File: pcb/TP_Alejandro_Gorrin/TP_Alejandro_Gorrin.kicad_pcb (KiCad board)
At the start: 2 copper layers, 33 parts, among them J1 Conn_01x12, J2 Conn_01x02, J3 Conn_01x16, J4 USB_A, Q1 MMBT3904, Q2 MMBT3904, Q3 BS250, SW1 SW_1, U1 MCP73831-2-OT, U3 CP2104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

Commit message: Empezando con el ruteo
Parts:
- moved U4 61.7 mm to (129.0, 88.0)
- moved J3 56.7 mm to (147.0, 123.0), turned to 90 degrees
- moved C6 53.7 mm to (128.0, 82.0), turned to 270 degrees
- moved R13 51.0 mm to (155.0, 82.0)
- moved C1 47.6 mm to (128.0, 105.0), turned to 90 degrees
- moved Q2 44.7 mm to (145.0, 115.0), turned to 90 degrees
- moved C2 44.7 mm to (123.5, 113.0), turned to 180 degrees
- moved D4 39.2 mm to (133.0, 82.0), turned to 270 degrees
- moved HS1 37.7 mm to (175.0, 110.0), turned to 270 degrees
- moved R4 36.4 mm to (151.7, 92.0)
- moved U5 36.3 mm to (155.0, 100.0)
- moved R3 34.8 mm to (147.0, 92.0)
- moved J2 31.3 mm to (144.0, 83.0), turned to 90 degrees
- moved R7 30.2 mm to (124.0, 88.3), turned to 270 degrees
- moved R10 29.2 mm to (159.3, 110.0), turned to 180 degrees
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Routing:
- net GNDD: track 0.00 -> 54.6 mm
- net +3V3: track 0.00 -> 26.9 mm
- net /RESET: track 0.00 -> 10.2 mm
- net +BATT: track 0.00 -> 9.84 mm
- net Net-(Q2-Pad1): track 0.00 -> 7.39 mm
- net Net-(R1-Pad2): track 0.00 -> 7.19 mm
- net VBUS: track 0.00 -> 5.75 mm
- net Net-(Q1-Pad1): track 0.00 -> 5.23 mm
- net /RTS: track 0.00 -> 4.62 mm
- net Net-(C6-Pad1): track 0.00 -> 4.29 mm
- net Net-(D1-Pad1): track 0.00 -> 4.17 mm
- net /A13_I35: track 0.00 -> 4.04 mm
- net Net-(R7-Pad2): track 0.00 -> 4.03 mm
- net /DTR: track 0.00 -> 3.73 mm
- net Net-(D3-Pad2): track 0.00 -> 3.03 mm
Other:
- board outline added: 79 x 47 mm
- net class Prueba added: clearance 0.8, trace_width 0.8, via_dia 1.6, via_drill 0.8

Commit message: vias del PCB
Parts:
- moved U5 1.41 mm to (156.0, 101.0), turned to 270 degrees
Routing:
- net VBUS: track 5.75 -> 106.8 mm, vias 0 -> 9
- net GNDD: track 54.6 -> 124.4 mm, vias 0 -> 9
- net +BATT: track 9.84 -> 77.7 mm, vias 0 -> 3
- net +3V3: track 26.9 -> 74.2 mm, vias 0 -> 3
- net /RESET: track 10.2 -> 43.6 mm, vias 0 -> 1
- net /RTS: track 4.62 -> 33.1 mm, vias 0 -> 2
- net /DTR: track 3.73 -> 29.4 mm
- net Net-(J4-Pad2): track 0.00 -> 22.8 mm, vias 0 -> 1
- net Net-(J4-Pad3): track 0.00 -> 21.6 mm, vias 0 -> 1
- net Net-(C6-Pad1): track 4.29 -> 23.0 mm, vias 0 -> 1
- net Net-(J4-Pad5): track 0.00 -> 13.1 mm
- net Net-(R2-Pad1): track 0.00 -> 6.94 mm, vias 0 -> 2

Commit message: Cambios del Esquematico
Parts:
- C1: footprint Connector_USB:USB_A_CONNFLY_DS1095-WNR0 -> Capacitor_SMD:C_0805_2012Metric
- C2, C3, C4, C6, C7, C8: footprint Capacitor_SMD:CP_Elec_3x5.3 -> Capacitor_SMD:C_0805_2012Metric
- D1, D3, D4: footprint LED_SMD:LED_0603_1608Metric -> LED_SMD:LED_0805_2012Metric
- R1, R10, R12, R13, R13G1, R13G2, R2, R3, R4, R7: footprint Resistor_SMD:R_0201_0603Metric -> Resistor_SMD:R_0805_2012Metric
- SW1: footprint Button_Switch_SMD:SW_DIP_SPSTx01_Slide_6.7x4.1mm_W6.73mm_P2.54mm_LowProfile_JPin -> Button_Switch_SMD:SW_Push_1P1T_NO_6x6mm_H9.5mm
- U5: value ESP3212 -> ESP32-WROOM; footprint ESP32-footprints-Lib:ESP32 -> ESP32-footprints-Lib:ESP32-WROOM
- moved D1 79.5 mm to (198.1, 65.1), turned to 0 degrees
- moved R13G2 73.0 mm to (202.5, 65.1), turned to 0 degrees
- moved R13G1 70.5 mm to (198.1, 68.1)
- moved D4 61.2 mm to (193.5, 72.3), turned to 0 degrees
- moved J3 60.8 mm to (126.0, 65.9), turned to 0 degrees
- moved J2 52.4 mm to (193.6, 65.9), turned to 0 degrees
- moved R12 49.6 mm to (176.6, 92.9)
- moved R10 48.7 mm to (193.4, 75.3), turned to 0 degrees
- moved R7 43.8 mm to (164.7, 104.3), turned to 0 degrees
- moved U4 43.4 mm to (172.0, 93.7)
- moved R1 39.5 mm to (164.7, 98.4)
- moved HS1 38.2 mm to (155.2, 77.3), turned to 0 degrees
- moved R2 38.1 mm to (171.8, 97.5)
- moved U5 33.4 mm to (180.3, 78.1), turned to 0 degrees
- moved C1 32.3 mm to (160.3, 104.5), turned to 0 degrees
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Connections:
- R1 pad 1: GNDD -> Net-(R1-Pad1)
- R1 pad 2: Net-(R1-Pad2) -> GNDD
- U1 pad 5: Net-(R1-Pad2) -> Net-(R1-Pad1)
- U5 pad 10: /A0_DAC2 -> /A1_DAC1
- U5 pad 11: /IO27_A10 -> /A0_DAC2
- U5 pad 12: /IO14_A6 -> /IO27_A10
- U5 pad 13: /IO12_A11 -> /IO14_A6
- U5 pad 14: /IO13_A12 -> /IO12_A11
- U5 pad 15: /IO15_A8 -> GNDD
- U5 pad 16: Net-(U5-Pad16) -> /IO13_A12
- U5 pad 17: /GPIO2 -> Net-(U5-Pad17)
- U5 pad 18: /GPIO0 -> Net-(U5-Pad18)
- U5 pad 19: /A5_IO4 -> Net-(U5-Pad19)
- U5 pad 2: /RESET -> +3V3
- U5 pad 20: /IO16 -> Net-(U5-Pad20)
- U5 pad 21: +3V3 -> Net-(U5-Pad21)
- U5 pad 22: /IO17 -> Net-(U5-Pad22)
- U5 pad 23: /SCK -> /IO15_A8
- U5 pad 24: /MISI -> /GPIO2
- U5 pad 25: /SDA -> /GPIO0
- U5 pad 26: /MISO -> /A5_IO4
- U5 pad 27: /SCI -> /IO16
- U5 pad 28: /RXD0 -> /IO17
- U5 pad 29: /TXD0 -> /SCK
- U5 pad 3: /A4_IO36 -> /RESET
- U5 pad 30: /IO21 -> /MISI
- U5 pad 31: Net-(U5-Pad31) -> /MISO
- U5 pad 32: (no net) -> Net-(U5-Pad32)
- U5 pad 33: (no net) -> /IO21
- U5 pad 34: (no net) -> /RXD0
- U5 pad 35: (no net) -> /TXD0
- U5 pad 36: (no net) -> /SCI
- U5 pad 37: (no net) -> /SDA
- U5 pad 38: (no net) -> Net-(U5-Pad38)
- U5 pad 39: (no net) -> Net-(U5-Pad39)
- U5 pad 4: /A3_I39 -> /A4_IO36
- U5 pad 5: /A2_I34 -> /A3_I39
- U5 pad 6: /A13_I35 -> /A2_I34
- U5 pad 7: /IO32_A7 -> /A13_I35
- U5 pad 8: /IO33_A9 -> /IO32_A7
- U5 pad 9: /A1_DAC1 -> /IO33_A9
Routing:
- net GNDD: track 124.4 -> 0.00 mm, vias 9 -> 0
- net VBUS: track 106.8 -> 0.00 mm, vias 9 -> 0
- net +BATT: track 77.7 -> 0.00 mm, vias 3 -> 0
- net +3V3: track 74.2 -> 0.00 mm, vias 3 -> 0
- net /RESET: track 43.6 -> 0.00 mm, vias 1 -> 0
- net /RTS: track 33.1 -> 0.00 mm, vias 2 -> 0
- net /DTR: track 29.4 -> 0.00 mm
- net Net-(C6-Pad1): track 23.0 -> 0.00 mm, vias 1 -> 0
- net Net-(J4-Pad2): track 22.8 -> 0.00 mm, vias 1 -> 0
- net Net-(J4-Pad3): track 21.6 -> 0.00 mm, vias 1 -> 0
- net Net-(J4-Pad5): track 13.1 -> 0.00 mm
- net Net-(Q2-Pad1): track 7.39 -> 0.00 mm
- net Net-(R1-Pad2): track 7.19 -> 0.00 mm
- net Net-(R2-Pad1): track 6.94 -> 0.00 mm, vias 2 -> 0
- net Net-(Q1-Pad1): track 5.23 -> 0.00 mm
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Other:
- board outline removed
- net class Default: clearance 0.2 -> 0.1
- rule trace_clearance: 0.2 -> 0.1

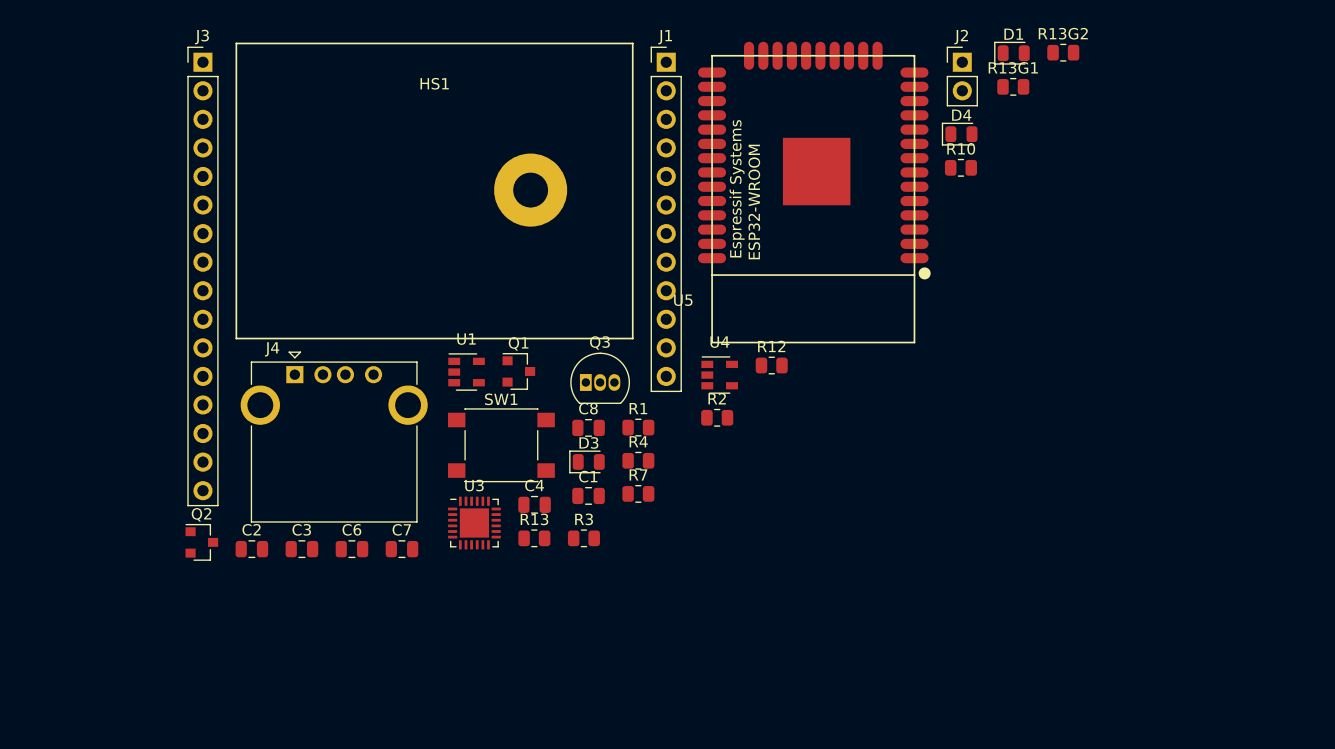
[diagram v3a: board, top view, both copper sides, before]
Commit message: Agrego avances de PCB, problemas con el heatsink
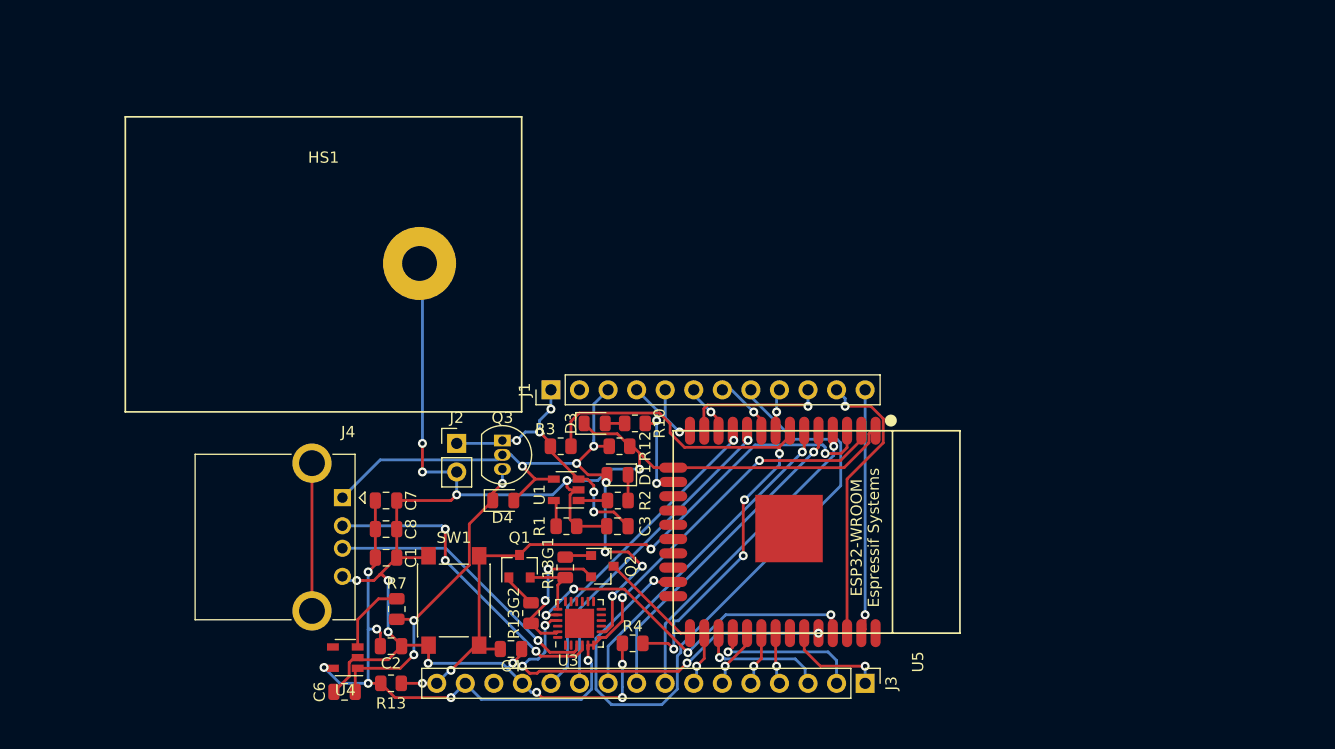
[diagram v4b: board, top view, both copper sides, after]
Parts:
- moved J3 80.7 mm to (184.9, 121.2), turned to 270 degrees
- moved R13G2 68.7 mm to (155.2, 114.9), turned to 270 degrees
- moved R13G1 58.4 mm to (158.2, 110.8), turned to 270 degrees
- moved J2 56.3 mm to (148.6, 99.8)
- moved D4 52.2 mm to (152.7, 104.9)
- moved D1 51.5 mm to (162.9, 102.6), turned to 180 degrees
- moved U4 41.7 mm to (138.7, 118.9), turned to 180 degrees
- moved R10 36.8 mm to (164.4, 98.0)
- moved Q2 35.7 mm to (161.5, 110.7)
- moved J1 30.9 mm to (157.0, 95.1), turned to 90 degrees
- moved U5 29.6 mm to (180.6, 107.7), turned to 90 degrees
- moved C3 28.1 mm to (162.9, 107.2)
- moved R7 23.8 mm to (143.3, 114.6), turned to 90 degrees
- moved C8 20.1 mm to (142.3, 107.4)
- moved C1 18.8 mm to (142.3, 110.0)
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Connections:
- R10 pad 2: /IO13_A1 -> /IO13_A12
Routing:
- net GNDD: track 0.00 -> 145.7 mm, vias 0 -> 13
- net +3V3: track 0.00 -> 84.5 mm, vias 0 -> 8
- net /IO15_A8: track 0.00 -> 60.2 mm, vias 0 -> 2
- net VBUS: track 0.00 -> 59.7 mm, vias 0 -> 7
- net /RESET: track 0.00 -> 57.8 mm, vias 0 -> 4
- net /A13_I35: track 0.00 -> 49.7 mm, vias 0 -> 4
- net /RXD0: track 0.00 -> 34.3 mm, vias 0 -> 4
- net /TXD0: track 0.00 -> 32.8 mm, vias 0 -> 4
- net /A2_I34: track 0.00 -> 29.7 mm, vias 0 -> 1
- net /A0_DAC2: track 0.00 -> 29.2 mm, vias 0 -> 1
- net /A3_I39: track 0.00 -> 29.2 mm, vias 0 -> 1
- net Net-(C6-Pad1): track 0.00 -> 29.0 mm, vias 0 -> 3
- net /A4_IO36: track 0.00 -> 28.7 mm, vias 0 -> 1
- net /A1_DAC1: track 0.00 -> 28.7 mm, vias 0 -> 1
- net Net-(J4-Pad2): track 0.00 -> 28.4 mm, vias 0 -> 3
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
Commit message: PCB
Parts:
- moved C2 53.6 mm to (195.3, 107.3), turned to 90 degrees
- moved U4 53.5 mm to (185.9, 93.7), turned to 90 degrees
- moved R13 50.6 mm to (189.8, 102.6)
- moved C7 50.5 mm to (192.5, 99.6), turned to 270 degrees
- moved C6 48.5 mm to (180.8, 98.0), turned to 90 degrees
- moved C8 48.3 mm to (190.0, 99.6), turned to 270 degrees
- moved R7 47.5 mm to (187.7, 97.9)
- moved J2 46.2 mm to (194.6, 95.5), turned to 270 degrees
- moved C1 45.1 mm to (186.9, 103.7), turned to 270 degrees
- moved C4 38.7 mm to (189.8, 104.9), turned to 180 degrees
- moved SW1 38.7 mm to (186.9, 111.3)
- moved R3 37.5 mm to (195.3, 99.4), turned to 270 degrees
- moved J4 37.5 mm to (175.8, 101.5)
- moved U3 34.9 mm to (194.3, 113.3), turned to 270 degrees
- moved R4 34.3 mm to (195.3, 103.2), turned to 270 degrees
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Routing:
- net /IO15_A8: track 60.2 -> 22.9 mm, vias 2 -> 1
- net /TXD0: track 32.8 -> 0.00 mm, vias 4 -> 0
- net /A13_I35: track 49.7 -> 19.4 mm, vias 4 -> 2
- net /A2_I34: track 29.7 -> 0.00 mm, vias 1 -> 0
- net /A0_DAC2: track 29.2 -> 0.00 mm, vias 1 -> 0
- net /A3_I39: track 29.2 -> 0.00 mm, vias 1 -> 0
- net /A4_IO36: track 28.7 -> 0.00 mm, vias 1 -> 0
- net /A1_DAC1: track 28.7 -> 0.00 mm, vias 1 -> 0
- net /SCI: track 26.0 -> 0.00 mm, vias 1 -> 0
- net /SDA: track 21.8 -> 0.00 mm, vias 1 -> 0
- net +3V3: track 84.5 -> 68.8 mm, vias 8 -> 3
- net /RXD0: track 34.3 -> 19.2 mm, vias 4 -> 2
- net /GPIO0: track 9.26 -> 24.0 mm, vias 0 -> 2
- net GNDD: track 145.7 -> 131.1 mm, vias 13 -> 10
- net /IO17: track 13.8 -> 0.00 mm, vias 1 -> 0
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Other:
- net class Default: clearance 0.1 -> 0.2
- rule trace_clearance: 0.1 -> 0.2

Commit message: Avances PCB
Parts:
- removed HS1: Heatsink_Pad, Heatsink:Heatsink_35x26mm_1xFixation3mm_Fischer-SK486-35
- J4: value USB_A -> USB_B_Micro; footprint Connector_USB:USB_A_CONNFLY_DS1095-WNR0 -> Connector_USB:USB_Micro-B_Molex_47346-0001
- moved J2 60.2 mm to (135.4, 84.3)
- moved C3 54.5 mm to (129.5, 85.0)
- moved C1 50.0 mm to (137.4, 96.6)
- moved C2 50.0 mm to (145.8, 100.1)
- moved C4 50.0 mm to (140.3, 97.8)
- moved C7 50.0 mm to (143.0, 92.5)
- moved C8 50.0 mm to (140.5, 92.5)
- moved D3 50.0 mm to (143.3, 100.2)
- moved J1 50.0 mm to (140.2, 84.3)
- moved J3 50.0 mm to (130.0, 111.8)
- moved Q1 50.0 mm to (132.1, 103.9)
- moved Q2 50.0 mm to (129.8, 107.7)
- moved R10 50.0 mm to (143.3, 96.4)
- moved R13 50.0 mm to (140.3, 95.5)
- moved R13G1 50.0 mm to (132.8, 107.8)
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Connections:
- J4 pad 4: GNDD -> Net-(J4-Pad4)
- J4 pad 5: Net-(J4-Pad5) -> GNDD
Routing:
- net Net-(J4-Pad5): track 13.1 -> 0.00 mm
- net Net-(J4-Pad6): track 0.00 -> 12.6 mm
- net VBUS: track 57.8 -> 46.8 mm, vias 8 -> 7
- net +3V3: track 68.8 -> 59.0 mm
- net Net-(R1-Pad1): track 2.80 -> 10.5 mm, vias 0 -> 2
- net Net-(D1-Pad1): track 1.93 -> 9.01 mm, vias 0 -> 2
- net +BATT: track 37.7 -> 43.4 mm, vias 2 -> 3
- net Net-(R7-Pad2): track 2.54 -> 7.99 mm, vias 0 -> 2
- net Net-(R2-Pad1): track 10.7 -> 15.7 mm
- net Net-(Q1-Pad1): track 7.02 -> 2.11 mm
- net Net-(J4-Pad3): track 23.0 -> 20.9 mm, vias 1 -> 2
- net Net-(J4-Pad2): track 22.0 -> 20.0 mm, vias 1 -> 2
- net GNDD: track 131.1 -> 129.6 mm, vias 10 -> 6
- net /DTR: track 25.5 -> 26.9 mm
- net Net-(C6-Pad1): track 18.8 -> 19.3 mm

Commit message: PCB conexiones realizadas
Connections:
- J1 pad 10: /IO14_A6 -> /A2_I34
- J1 pad 11: /SCI -> /A3_I39
- J1 pad 12: /SDA -> /A4_IO36
- J1 pad 2: /EN -> VBUS
- J1 pad 3: VBUS -> /IO12_A11
- J1 pad 4: /IO13_A12 -> /IO14_A6
- J1 pad 5: /IO12_A11 -> /IO27_A10
- J1 pad 6: /IO27_A10 -> /A0_DAC2
- J1 pad 7: /IO33_A9 -> /A1_DAC1
- J1 pad 8: /IO15_A8 -> /IO33_A9
- J3 pad 1: /IO21 -> +3V3
- J3 pad 10: /A2_I34 -> /IO17
- J3 pad 11: /A1_DAC1 -> /SCK
- J3 pad 12: /A0_DAC2 -> /MISI
- J3 pad 13: GNDD -> /MISO
- J3 pad 14: Net-(J3-Pad14) -> /IO21
- J3 pad 15: +3V3 -> /SCI
- J3 pad 16: /RESET -> /SDA
- J3 pad 2: /IO17 -> /RESET
- J3 pad 3: /IO16 -> GNDD
- J3 pad 4: /MISO -> /EN
- J3 pad 5: /MISI -> Net-(J3-Pad5)
- J3 pad 6: /SCK -> /IO13_A12
- J3 pad 7: /A5_IO4 -> /IO15_A8
- J3 pad 8: /A4_IO36 -> /A5_IO4
- J3 pad 9: /A3_I39 -> /IO16
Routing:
- net GNDD: track 129.6 -> 99.1 mm
- net +3V3: track 59.0 -> 86.1 mm, vias 3 -> 6
- net /TXD0: track 0.00 -> 21.0 mm, vias 0 -> 2
- net /IO13_A12: track 18.8 -> 35.7 mm, vias 2 -> 5
- net /IO14_A6: track 17.7 -> 6.91 mm
- net /RESET: track 49.6 -> 59.4 mm, vias 2 -> 3
- net /A4_IO36: track 0.00 -> 8.57 mm, vias 0 -> 1
- net /A5_IO4: track 0.00 -> 7.65 mm, vias 0 -> 1
- net /IO15_A8: track 22.9 -> 15.4 mm, vias 1 -> 3
- net /A3_I39: track 0.00 -> 7.20 mm, vias 0 -> 1
- net /IO16: track 0.00 -> 6.11 mm, vias 0 -> 1
- net /IO17: track 0.00 -> 5.52 mm, vias 0 -> 1
- net /A0_DAC2: track 0.00 -> 5.52 mm, vias 0 -> 1
- net /IO21: track 0.00 -> 5.49 mm, vias 0 -> 1
- net /A2_I34: track 0.00 -> 5.49 mm, vias 0 -> 1
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
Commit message: Cambio y agrego vias para facilitar el ruteo
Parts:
- added MK101: MountingHole, MountingHole:MountingHole_2.2mm_M2_DIN965_Pad, F.Cu at (126.0, 87.9)
- added MK102: MountingHole, MountingHole:MountingHole_2.2mm_M2_DIN965_Pad, F.Cu at (125.0, 107.7)
- added MK103: MountingHole, MountingHole:MountingHole_2.2mm_M2_DIN965_Pad, F.Cu at (173.0, 86.1)
- added MK104: MountingHole, MountingHole:MountingHole_2.2mm_M2_DIN965_Pad, F.Cu at (172.7, 110.2)
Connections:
- J4 pad 5: GNDD -> Net-(J4-Pad5)
